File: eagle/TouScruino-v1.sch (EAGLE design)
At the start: 47 parts, among them J1 AVR_ISP, Q1 8MHz, Q2 MMBT2222, Q3 8MHz, U1 ATMEGA1284P, U3 ARDUINO_SHIELD, U4 MCP73831, U5 MIC5209-3.3YS, X1 USBSMD

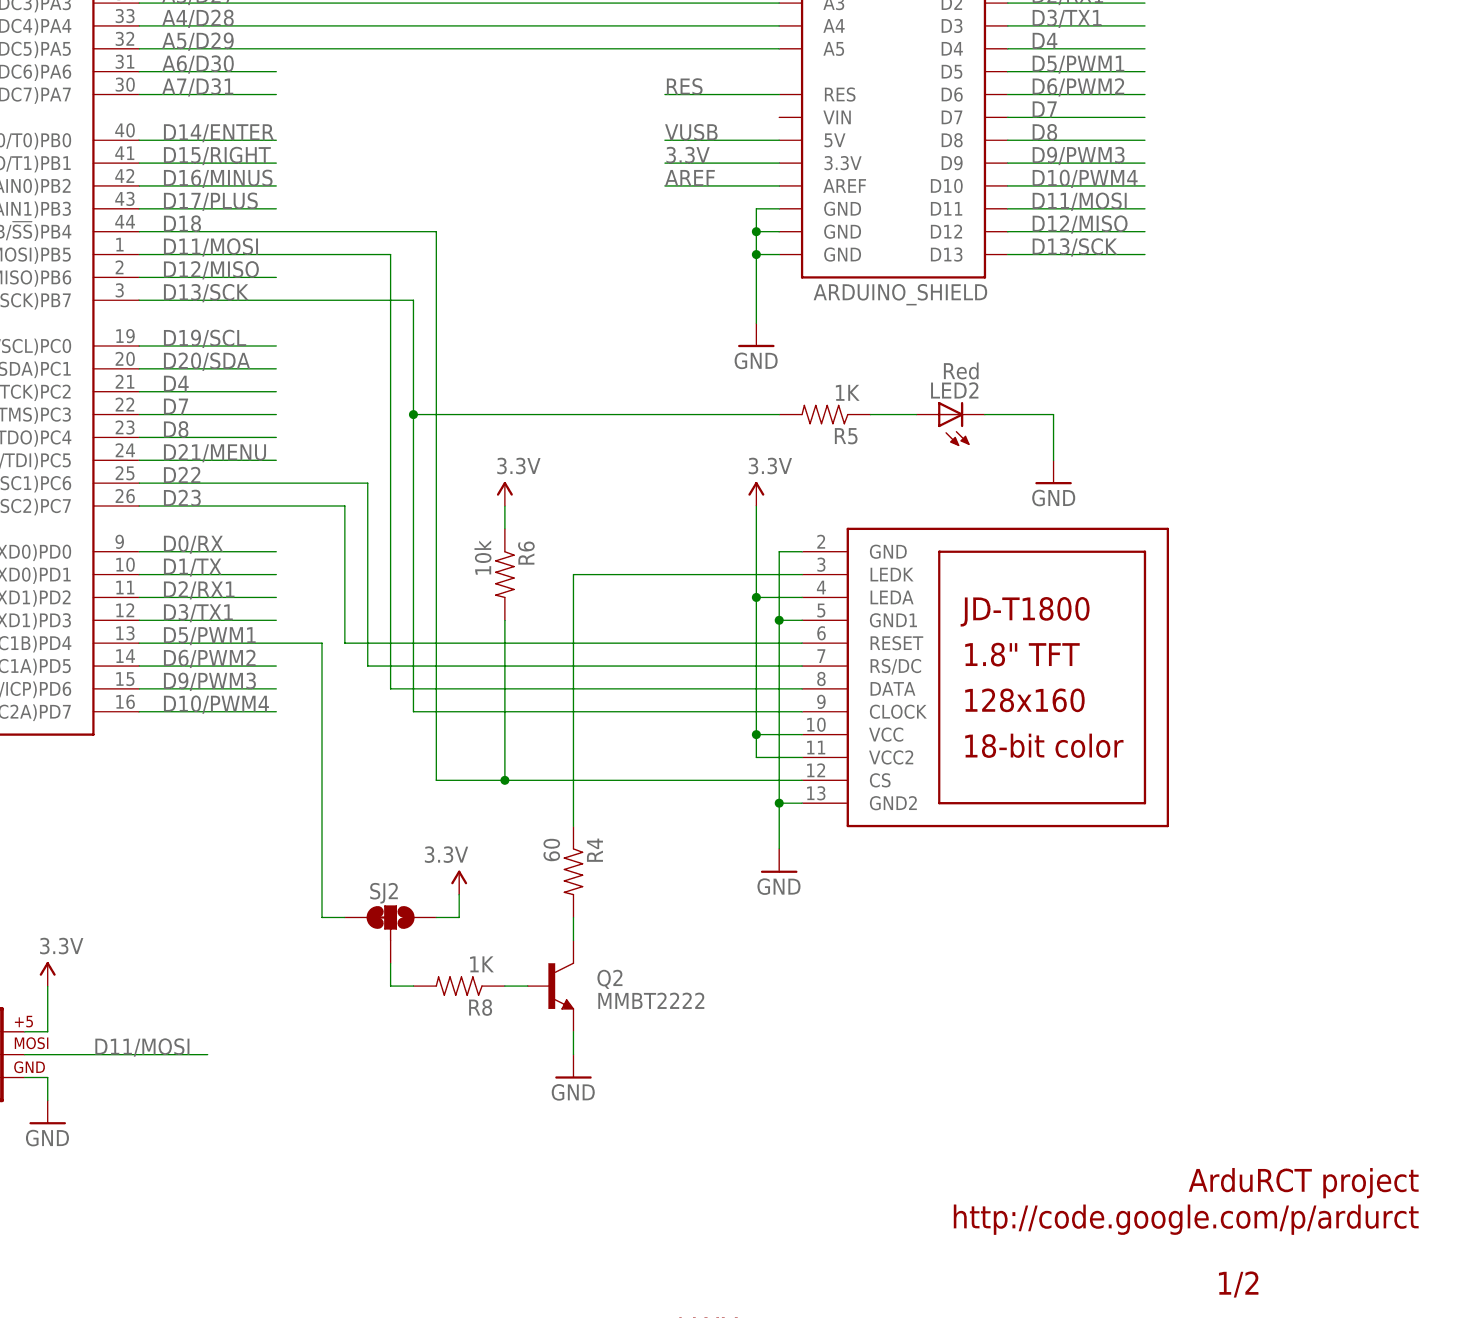
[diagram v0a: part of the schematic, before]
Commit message: 
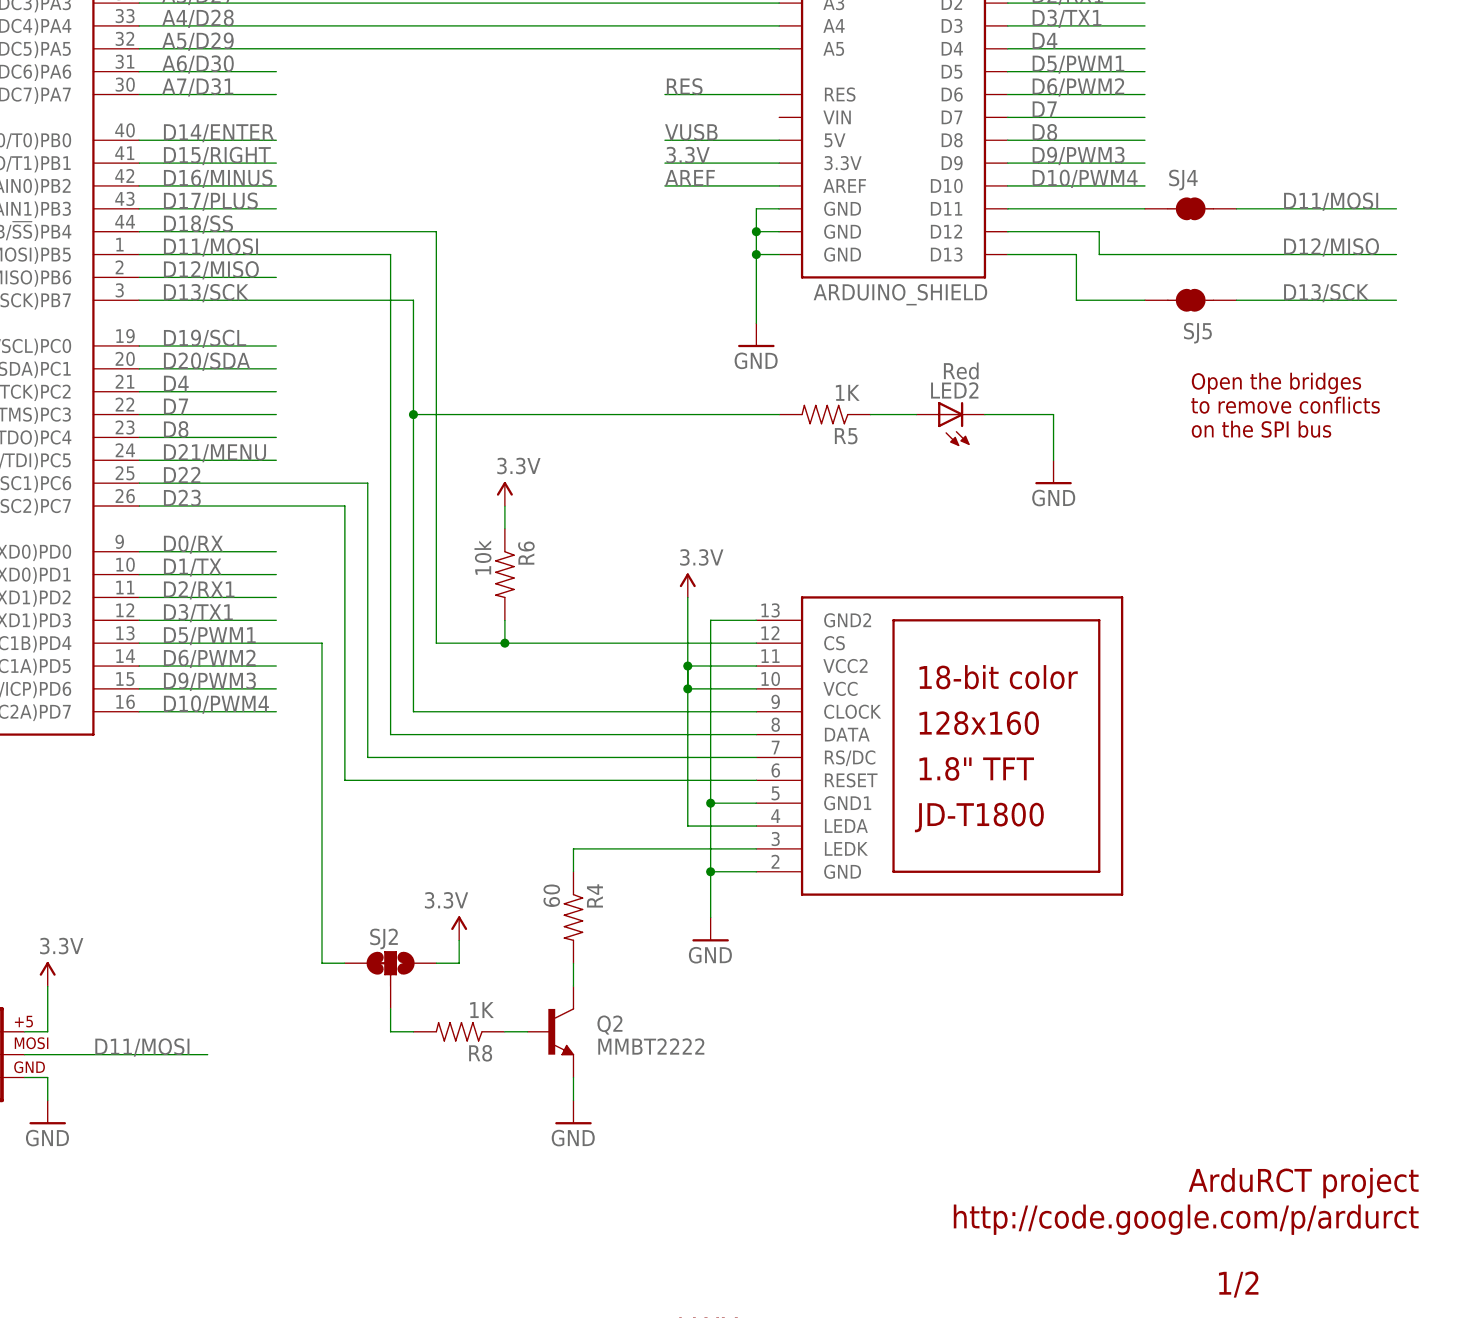
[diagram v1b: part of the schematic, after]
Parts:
- added SJ4, SJ5: SOLDERJUMPERTRACE, SparkFun:SOLDERJUMPERTRACE
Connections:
- net D18 renamed D18/SS
- new net N$6: SJ4.1, U3.D11
- new net N$9: SJ5.2, U3.D13
- net D11/MOSI: now also SJ4.2; no longer U3.D11
- net D13/SCK: now also SJ5.1; no longer U3.D13
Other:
- note added: "Open the bridges to remove conflicts on the SPI bus"
- moved on the sheet: Q2, R4, R8, SJ2
